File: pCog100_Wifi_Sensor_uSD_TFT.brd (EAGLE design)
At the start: 48 x 28 mm, 23 parts

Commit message: Update all of the Fonts and graphics
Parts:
- added U$11, U$12, U$6: (no value), GadgetFactory:GADGETBOX_SMALL
- added U$13, U$14, U$15, U$16, U$17: (no value), ohw-logo:OSHW_FILLX150_NOTEXT
- moved U$1 1.70 mm to (72.4, 46.3)
- moved U$10 1.27 mm to (25.1, 8.95)
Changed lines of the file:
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@@
 <setting verticaltext="up"/>
 </settings>
-<grid distance="1" unitdist="mm" unit="mm" style="lines" multiple="1" display="yes" altdistance="0.1" altunitdist="mm" altunit="mm"/>
+<grid distance="0.05" unitdist="inch" unit="inch" style="lines" multiple="1" display="yes" altdistance="0.005" altunitdist="inch" altunit="inch"/>
 <layers>
-<layer number="1" name="Top" color="4" fill="1" visible="yes" active="yes"/>
+<layer number="1" name="Top" color="4" fill="1" visible="no" active="yes"/>
 <layer number="2" name="Route2" color="1" fill="3" visible="no" active="yes"/>
 <layer number="3" name="Route3" color="4" fill="3" visible="no" active="yes"/>
 <layer number="14" name="Route14" color="1" fill="6" visible="no" active="yes"/>
 <layer number="15" name="Route15" color="4" fill="6" visible="no" active="yes"/>
-<layer number="16" name="Bottom" color="1" fill="1" visible="yes" active="yes"/>
+<layer number="16" name="Bottom" color="1" fill="1" visible="no" active="yes"/>
 <layer number="17" name="Pads" color="2" fill="1" visible="yes" active="yes"/>
 <layer number="18" name="Vias" color="2" fill="1" visible="yes" active="yes"/>
@@
 <layer number="20" name="Dimension" color="15" fill="1" visible="yes" active="yes"/>
 <layer number="21" name="tPlace" color="16" fill="1" visible="yes" active="yes"/>
-<layer number="22" name="bPlace" color="14" fill="1" visible="yes" active="yes"/>
+<layer number="22" name="bPlace" color="14" fill="1" visible="no" active="yes"/>
 <layer number="23" name="tOrigins" color="15" fill="1" visible="yes" active="yes"/>
-<layer number="24" name="bOrigins" color="15" fill="1" visible="yes" active="yes"/>
+<layer number="24" name="bOrigins" color="15" fill="1" visible="no" active="yes"/>
 <layer number="25" name="tNames" color="16" fill="1" visible="yes" active="yes"/>
 <layer number="26" name="bNames" color="7" fill="1" visible="no" active="yes"/>
@@
 <layer number="29" name="tStop" color="7" fill="3" visible="no" active="yes"/>
 <layer number="30" name="bStop" color="7" fill="6" visible="no" active="yes"/>
-<layer number="31" name="tCream" color="7" fill="4" visible="no" active="yes"/>
+<layer number="31" name="tCream" color="7" fill="4" visible="yes" active="yes"/>
 <layer number="32" name="bCream" color="7" fill="5" visible="no" active="yes"/>
 <layer number="33" name="tFinish" color="6" fill="3" visible="no" active="yes"/>
@@
 <attribute name="DIGIKEY" value="RMCF0805JT10K0CT-ND" x="71.495" y="31.556" size="1.778" layer="28" rot="MR0" display="off"/>
 </element>
-<element name="U$1" library="GadgetFactory" package="GADGETBOX_TEXT" value="" x="70.86" y="47.05"/>
+<element name="U$1" library="GadgetFactory" package="GADGETBOX_TEXT" value="" x="72.384" y="46.288"/>
 <element name="U$2" library="eCogs" package="LEGEND_DIO" value="" x="49.27" y="50.86"/>
 <element name="U$3" library="eCogs" package="LEGEND_DIO" value="" x="49.27" y="48.32"/>
@@
 <attribute name="DIGIKEY" value="RMCF0805JT47K0CT-ND" x="20.07" y="20.38" size="1.778" layer="28" rot="MR180" display="off"/>
 </element>
-<element name="U$10" library="GadgetFactory" package="GADGETBOX_TEXT" value="" x="25.15" y="7.68" rot="R180"/>
+<element name="U$10" library="GadgetFactory" package="GADGETBOX_TEXT" value="" x="25.15" y="8.95" rot="R180"/>
+<element name="U$6" library="GadgetFactory" package="GADGETBOX_SMALL" value="" x="19.05" y="53.34"/>
+<element name="U$11" library="GadgetFactory" package="GADGETBOX_SMALL" value="" x="26.67" y="30.48" rot="R180"/>
+<element name="U$12" library="GadgetFactory" package="GADGETBOX_SMALL" value="" x="88.646" y="11.049" rot="R90"/>
+<element name="U$13" library="ohw-logo" package="OSHW_FILLX150_NOTEXT" value="" x="89.154" y="36.195"/>
+<element name="U$14" library="ohw-logo" package="OSHW_FILLX150_NOTEXT" value="" x="94.869" y="7.366" rot="R90"/>
+<element name="U$15" library="ohw-logo" package="OSHW_FILLX150_NOTEXT" value="" x="6.731" y="19.685" rot="R180"/>
+<element name="U$16" library="ohw-logo" package="OSHW_FILLX150_NOTEXT" value="" x="32.004" y="50.927"/>
+<element name="U$17" library="ohw-logo" package="OSHW_FILLX150_NOTEXT" value="" x="12.573" y="32.766" rot="R180"/>
 </elements>
 <signals>

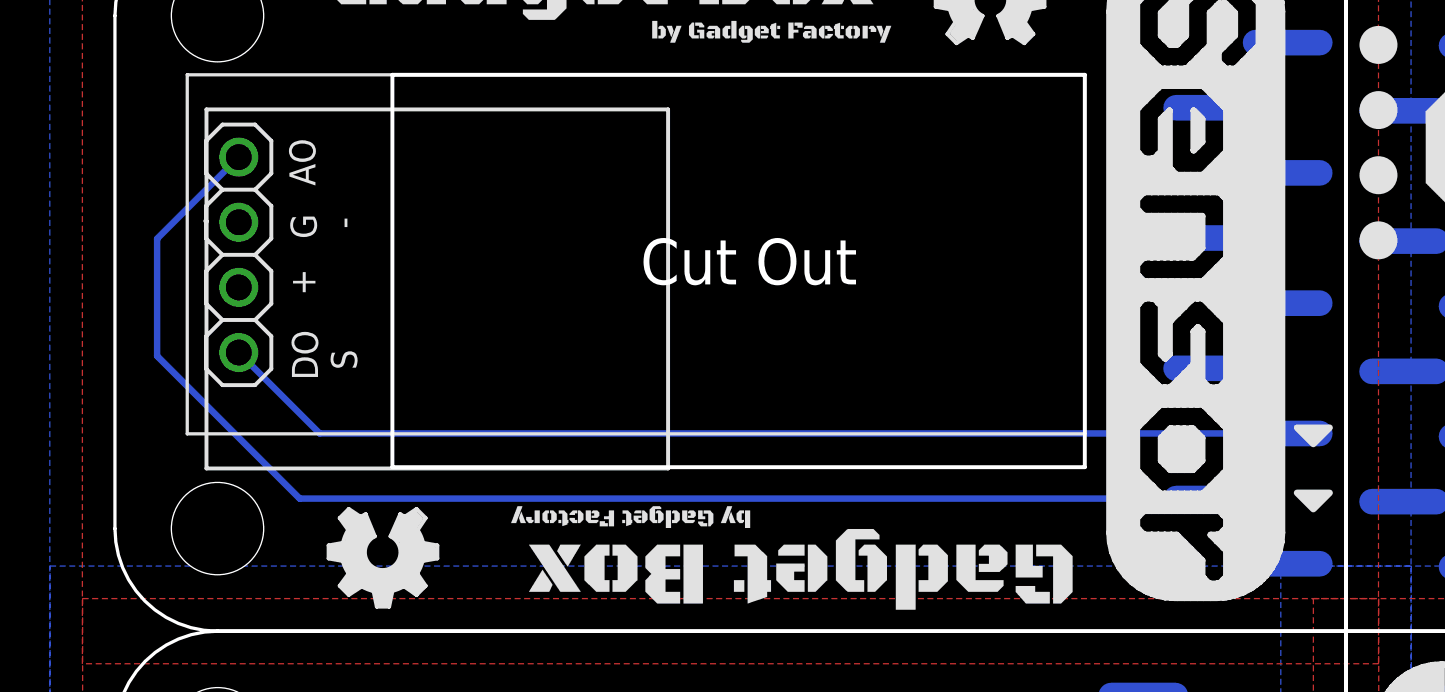
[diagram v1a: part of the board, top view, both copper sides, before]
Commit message: Fix a trace on the Sensor eCog that went through cutout.
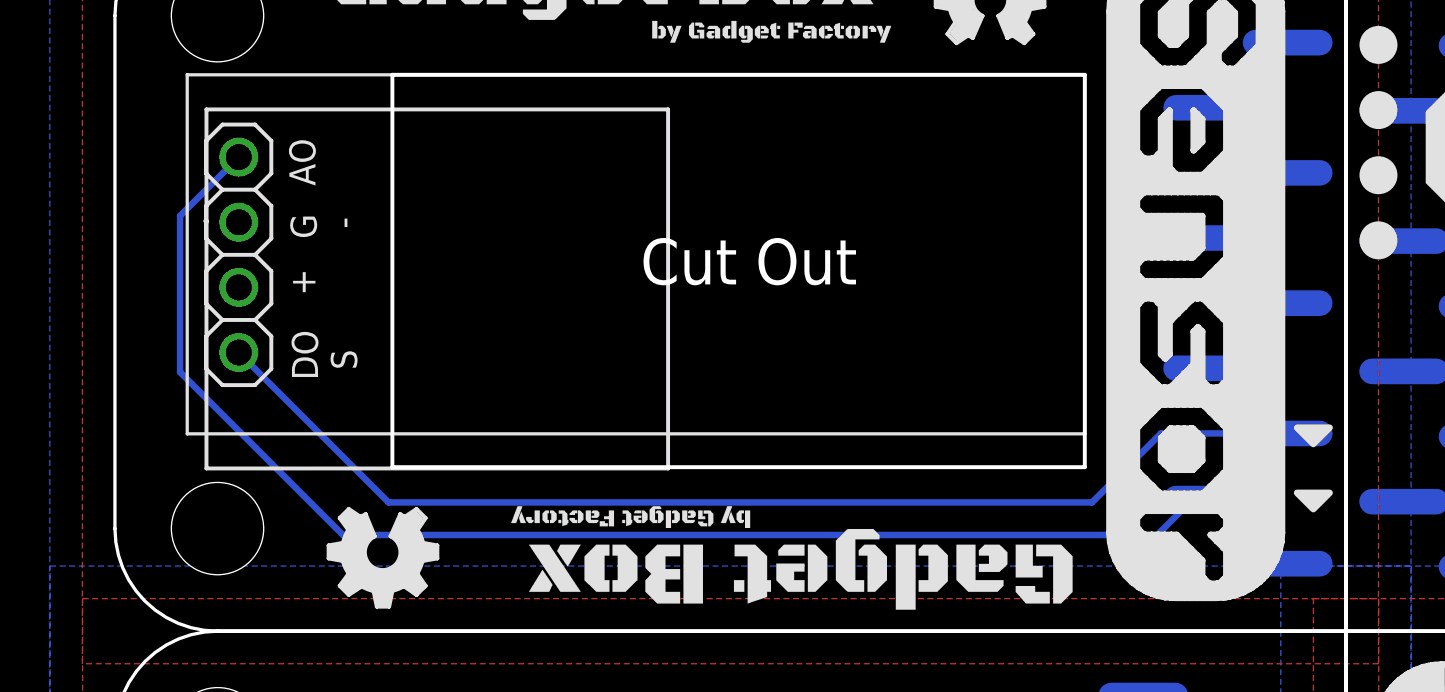
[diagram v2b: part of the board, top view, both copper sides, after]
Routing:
- net A2: track 42.2 -> 44.4 mm
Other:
- board text added: "ecog103 v1.2"
- board text removed: "ecog103 v1.1"
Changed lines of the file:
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@@
 <text x="61.795" y="24.892" size="1.016" layer="22" font="vector" rot="MR0">GND</text>
 <text x="16.471" y="29.585" size="0.8128" layer="22" font="vector" rot="MR180">ecog103.GadgetFactory.net</text>
-<text x="8.328" y="54.841" size="1.016" layer="22" font="vector" rot="MR180">ecog103 v1.1</text>
+<text x="8.328" y="54.841" size="1.016" layer="22" font="vector" rot="MR180">ecog103 v1.2</text>
 <text x="8.328" y="53.571" size="1.016" layer="22" font="vector" rot="MR180">Sensor</text>
 <text x="8.328" y="52.301" size="1.016" layer="22" font="vector" rot="MR180">eCogs</text>
@@
 <contactref element="U$7" pad="DO/S"/>
 <contactref element="ECOG2" pad="G1"/>
-<wire x1="45.7294" y1="35.71" x2="7.984" y2="35.71" width="0.254" layer="16"/>
-<wire x1="7.984" y1="35.71" x2="4.829" y2="38.865" width="0.254" layer="16"/>
+<wire x1="45.7294" y1="35.71" x2="40.79" y2="35.71" width="0.254" layer="16"/>
+<wire x1="40.79" y1="35.71" x2="38.1" y2="33.02" width="0.254" layer="16"/>
+<wire x1="38.1" y1="33.02" x2="10.674" y2="33.02" width="0.254" layer="16"/>
+<wire x1="10.674" y1="33.02" x2="4.829" y2="38.865" width="0.254" layer="16"/>
 </signal>
 <signal name="A1">
 <contactref element="U$7" pad="AO"/>
 <contactref element="ECOG2" pad="G0"/>
-<wire x1="42.6306" y1="33.17" x2="7.203" y2="33.17" width="0.254" layer="16"/>
-<wire x1="7.203" y1="33.17" x2="1.645" y2="38.728" width="0.254" layer="16"/>
-<wire x1="1.645" y1="38.728" x2="1.645" y2="43.301" width="0.254" layer="16"/>
-<wire x1="1.645" y1="43.301" x2="4.829" y2="46.485" width="0.254" layer="16"/>
+<wire x1="42.6306" y1="33.17" x2="42.06" y2="33.17" width="0.254" layer="16"/>
+<wire x1="42.06" y1="33.17" x2="40.64" y2="31.75" width="0.254" layer="16"/>
+<wire x1="40.64" y1="31.75" x2="8.89" y2="31.75" width="0.254" layer="16"/>
+<wire x1="8.89" y1="31.75" x2="2.54" y2="38.1" width="0.254" layer="16"/>
+<wire x1="2.54" y1="38.1" x2="2.54" y2="44.196" width="0.254" layer="16"/>
+<wire x1="2.54" y1="44.196" x2="4.829" y2="46.485" width="0.254" layer="16"/>
 </signal>
 <signal name="SD_MISO">

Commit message: All the 2.0 updates
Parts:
- removed U$17: (no value), ohw-logo:OSHW_FILLX150_NOTEXT
- ECOG: value ECOG_GENERAL_ROWECOG_GENERAL_SMD -> ECOG_BUSES_ROWECOG_BUSES_SMD; device eCogs:ECOG_GENERAL_SMD -> eCogs:ECOG_BUSES_SMD
- ECOG3: value ECOG_BUSES_ROWECOG_BUSES_SMD -> ECOG_GENERAL_ROWECOG_GENERAL_SMD; device eCogs:ECOG_BUSES_SMD -> eCogs:ECOG_GENERAL_SMD
- R1, R2, R3: value 10K -> 47K; device GadgetFactory:0805 -> GadgetFactory_6.0:0805
- R5, R6, R7: value 47K -> 10K; device GadgetFactory_6.0:0805 -> GadgetFactory:0805
- U$10: device GadgetFactory:GADGETBOX_TEXT -> GadgetFactory:GADGETBOX_SMALL
- U$11: device GadgetFactory:GADGETBOX_SMALL -> GadgetFactory:GADGETBOX_TEXT
- U$12: device GadgetFactory:GADGETBOX_SMALL -> eCogs:LEGEND_DIO
- U$13, U$14, U$15: device ohw-logo:OSHW_FILLX150_NOTEXT -> eCogs:LEGEND_DIO
- U$16: device ohw-logo:OSHW_FILLX150_NOTEXT -> ohw-logo:OSHW_FILLX200_NOTEXT
- U$2: device eCogs:LEGEND_DIO -> ohw-logo:OSHW_FILLX200_NOTEXT
- U$3: device eCogs:LEGEND_DIO -> GadgetFactory:GADGETBOX_SMALL
- U$4: device eCogs:LEGEND_DIO -> ohw-logo:OSHW_FILLX150_NOTEXT
- U$5: value (none) -> SENSOR; device eCogs:LEGEND_DIO -> eCogs:SENSOR-HJX4
- U$6: device GadgetFactory:GADGETBOX_SMALL -> eCogs:LEGEND_ANALOG
- U$7: value SENSOR -> (none); device eCogs:SENSOR-HJX4 -> eCogs:LEGEND_ANALOG
- U$8: device eCogs:LEGEND_ANALOG -> GadgetFactory:GADGETBOX_SMALL
- U$9: device eCogs:LEGEND_ANALOG -> ohw-logo:OSHW_FILLX150_NOTEXT
- moved U$14 61.5 mm to (49.0, 48.4), turned to 180 degrees
- moved R5 59.8 mm to (76.2, 32.0), turned to 0 degrees
- moved R7 58.3 mm to (68.7, 52.4)
- moved U$1 55.8 mm to (24.0, 18.4)
- moved ECOG1 55.6 mm to (96.0, 28.0), turned to 180 degrees
- moved ECOG 55.6 mm to (0.00, 0.00)
- moved ECOG3 55.6 mm to (96.0, 56.0)
- moved ECOG2 55.6 mm to (0.01, 28.0), turned to 0 degrees
- moved R6 55.4 mm to (63.4, 52.4)
- moved R2 55.2 mm to (27.9, 10.2), turned to 0 degrees
- moved R3 54.4 mm to (27.9, 7.62)
- moved R1 54.2 mm to (27.9, 16.5), turned to 0 degrees
- moved U$15 52.6 mm to (49.0, 50.9)
- moved U$3 51.9 mm to (88.6, 14.4), turned to 270 degrees
- moved U$4 51.6 mm to (90.7, 15.0), turned to 270 degrees
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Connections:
- removed net RX: ECOG.G1, X1.15
- removed net TX: ECOG.G0, X1.16
- new net RX/MOSI: ECOG3.G1, X1.15
- new net TX/MISO: ECOG3.G0, X1.16
- net 3V3: now also R2.2, U$5.+; no longer R5.2, U$7.+
- net A1: now also U$5.AO; no longer U$7.AO
- net A2: now also U$5.DO/S; no longer U$7.DO/S
- net GND: now also R5.1, U$5.GND; no longer R2.1, U$7.GND
- net GPIO0/BOOTLOAD: now also ECOG3.G2; no longer ECOG.G2
- net N$3: now also R4.1; no longer R1.1
- net N$4: now also R5.2; no longer R2.2
- net N$5: now also R7.1; no longer R4.1
- net RESET: now also ECOG3.G3, R6.1; no longer ECOG.G3, R3.1
- net SD_!CS: now also ECOG.SPI-CS, R3.1; no longer ECOG3.SPI-CS, R7.1
- net SD_MISO: now also ECOG.SPI-MISO, R1.1; no longer ECOG3.SPI-MISO, R5.1
- net SD_MOSI: now also ECOG.SPI-MOSI, R2.1; no longer ECOG3.SPI-MOSI, R6.1
- net SD_SCK: now also ECOG.SPI-SCK; no longer ECOG3.SPI-SCK
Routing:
- net 3V3: track 102.2 -> 147.2 mm, vias 7 -> 6
- net TX/MISO: track 0.00 -> 33.3 mm, vias 0 -> 2
- net RX: track 31.6 -> 0.00 mm
- net TX: track 29.6 -> 0.00 mm
- net RX/MOSI: track 0.00 -> 25.9 mm, vias 0 -> 2
- net A1: track 52.6 -> 40.1 mm
- net SD_MISO: track 40.9 -> 52.3 mm
- net SD_MOSI: track 55.7 -> 46.8 mm
- net SD_SCK: track 57.0 -> 48.5 mm
- net N$1: track 30.0 -> 22.1 mm
- net SD_!CS: track 55.3 -> 48.7 mm
- net RESET: track 37.3 -> 30.9 mm
- net GPIO0/BOOTLOAD: track 19.0 -> 22.9 mm
- net A2: track 44.4 -> 41.7 mm
- net N$2: track 30.6 -> 29.5 mm
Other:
- board size 48 x 28 mm -> 47.5 x 28 mm
- board text added: "0"
- board text added: "1"
- board text added: "2"
- board text added: "3"
- board text added: "RX/MOSI"
- board text added: "SPI-CS"
- board text added: "SPI-MISO"
- board text added: "SPI-MOSI"
- board text added: "SPI-SCK"
- board text added: "TX/MISO"
- board text added: "ecog100 v2.0"
- board text added: "ecog101 v2.0"
- board text added: "ecog102 v2.0"
- board text added: "ecog103 v2.0"
- board text removed: "RX>"
- board text removed: "SPI-CS>"
- board text removed: "SPI-MISO>"
- board text removed: "SPI-MOSI<"
- board text removed: "SPI-SCK>"
- board text removed: "TX<"
- board text removed: "ecog100 v1.1"
- board text removed: "ecog101 v1.1"
- board text removed: "ecog102 v1.1"
- board text removed: "ecog103 v1.2"
